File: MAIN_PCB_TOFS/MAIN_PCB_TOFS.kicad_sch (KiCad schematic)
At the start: 0 parts

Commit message: ajout de quelques éléments au pcb
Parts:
- added D4: GREEN_LED, LED_SMD:LED_0603_1608Metric, symbol Device:LED
- added D5: RED_LED, LED_SMD:LED_0603_1608Metric, symbol Device:LED
- added J1, J11, J2: Capteur Matricielle, Connector_PinHeader_2.54mm:PinHeader_1x07_P2.54mm_Vertical, symbol Connector_Generic:Conn_01x07
- added J12: SERVO m3, Connector_PinHeader_2.54mm:PinHeader_1x03_P2.54mm_Vertical, symbol Connector:Conn_01x03_Pin
- added J13: SERVO m4, Connector_PinHeader_2.54mm:PinHeader_1x03_P2.54mm_Vertical, symbol Connector:Conn_01x03_Pin
- added J3: SERVO m2, Connector_PinHeader_2.54mm:PinHeader_1x03_P2.54mm_Vertical, symbol Connector:Conn_01x03_Pin
- added J4: SERVO m1, Connector_PinHeader_2.54mm:PinHeader_1x03_P2.54mm_Vertical, symbol Connector:Conn_01x03_Pin
- added J5: COMM_inter_mcu, Connector_PinSocket_2.54mm:PinSocket_1x09_P2.54mm_Vertical, symbol Connector:Conn_01x09_Pin
- added R12, R13: 330R, Resistor_SMD:R_0603_1608Metric, symbol Device:R
- added U1: ESP32, composant_pami:esp32_wroom32, symbol ESP_32_ANGE:ESP_32_WROOM32
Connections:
- new net: D4.2 (A), R12.2
- new net: D5.2 (A), R13.2
- new net 3V3: J1.5 (Pin_5), J11.5 (Pin_5), J2.5 (Pin_5), J5.9 (Pin_9), U1.16 (3V3)
- new net 6V: J12.2 (Pin_2), J13.2 (Pin_2), J3.2 (Pin_2), J4.2 (Pin_2), J5.8 (Pin_8)
- new net CIN1: J5.6 (Pin_6), U1.10 (D32)
- new net CIN2: J5.5 (Pin_5), U1.9 (D33)
- new net D18: J12.1 (Pin_1), J3.1 (Pin_1)
- new net D19: J13.1 (Pin_1), J4.1 (Pin_1)
- new net DIN1: J5.4 (Pin_4), U1.8 (D25)
- new net DIN2: J5.3 (Pin_3), U1.7 (D26)
- new net GND: D4.1 (K), D5.1 (K), J1.7 (Pin_7), J11.7 (Pin_7), J12.3 (Pin_3), J13.3 (Pin_3), J2.7 (Pin_7), J3.3 (Pin_3), J4.3 (Pin_3), J5.7 (Pin_7), U1.17 (GND), U1.2 (GND)
- new net LED_IHM_1: R12.1, U1.6 (D27)
- new net LED_IHM_2: R13.1, U1.5 (D14)
- new net RX_ESP32: J5.2 (Pin_2), U1.21 (RX2)
- new net SCL: J1.2 (Pin_2), J11.2 (Pin_2), J2.2 (Pin_2), U1.29 (D22)
- new net SDA: J1.1 (Pin_1), J11.1 (Pin_1), J2.1 (Pin_1), U1.26 (D21)
- new net SERVO_1: U1.25 (D19)
- new net SERVO_2: U1.24 (D18)
- new net SERVO_3: U1.19 (D2)
- new net SERVO_4: U1.18 (D15)
- new net TX_ESP32: J5.1 (Pin_1), U1.22 (TX2)
- no-connect marks 0 -> 12
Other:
- note added: "Capteur TOF 1"
- note added: "Capteur TOF 2"
- note added: "Capteur TOF 3"
- note added: "Servo Moteur 1"
- note added: "Servo Moteur 2"
- note added: "Servo Moteur 3"
- note added: "Servo Moteur 4"

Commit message: début du schéma électrique
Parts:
- U1: footprint composant_pami:esp32_wroom32 -> Library:PinHeader_2x15_P2.54mm_Vertical_esp32
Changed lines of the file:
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@@
 			)
 		)
-		(property "Footprint" "composant_pami:esp32_wroom32"
+		(property "Footprint" "Library:PinHeader_2x15_P2.54mm_Vertical_esp32"
 			(at 85.09 44.45 0)
 			(effects

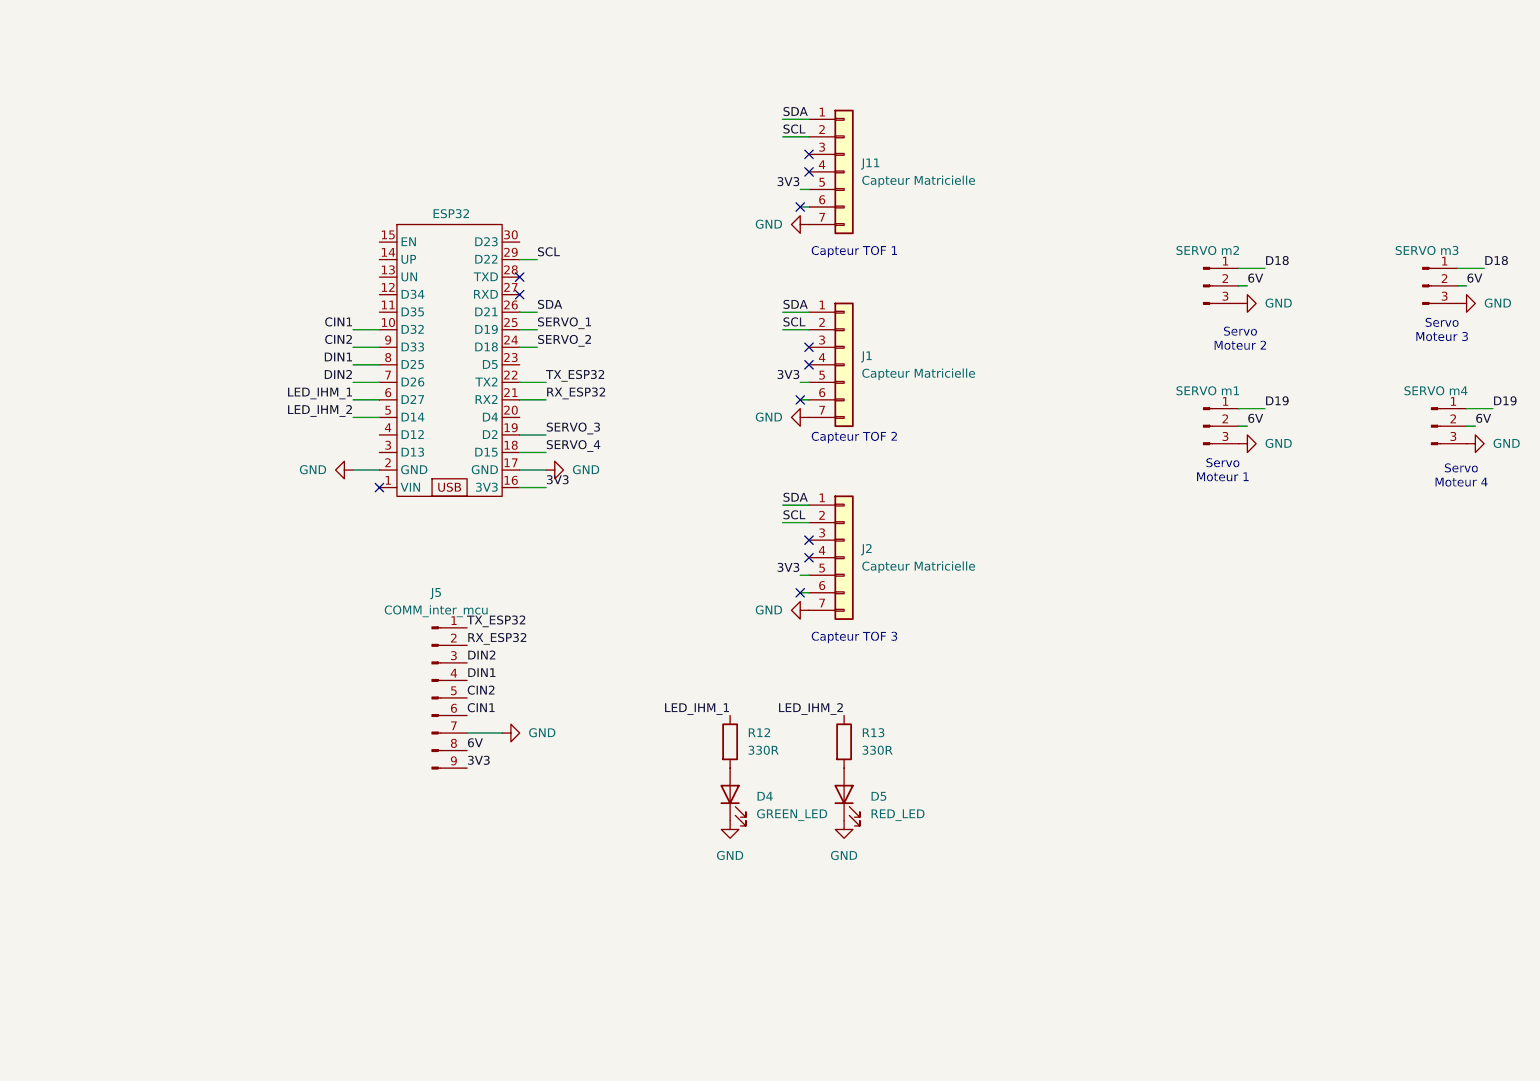
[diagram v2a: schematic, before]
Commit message: ajout des switch, des tofs et mise en place des capa de découplage sur le pcb logique
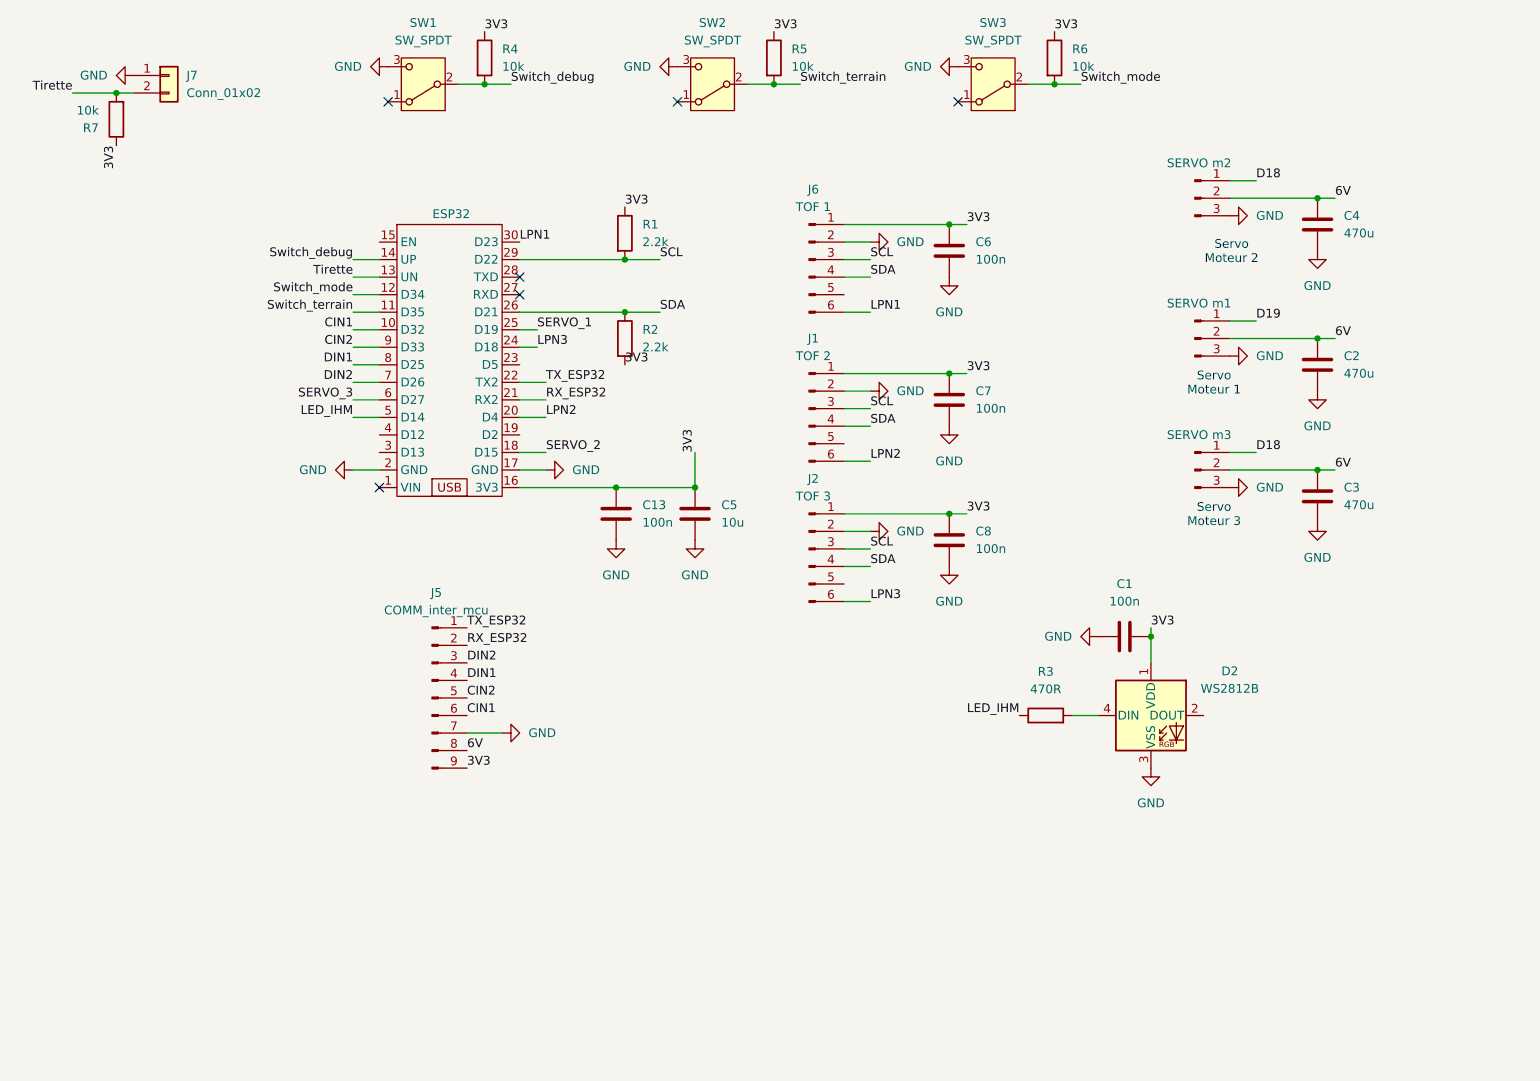
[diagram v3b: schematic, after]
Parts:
- removed D4: GREEN_LED, LED_SMD:LED_0603_1608Metric, symbol Device:LED
- removed D5: RED_LED, LED_SMD:LED_0603_1608Metric, symbol Device:LED
- removed J1, J11, J2: Capteur Matricielle, Connector_PinHeader_2.54mm:PinHeader_1x07_P2.54mm_Vertical, symbol Connector_Generic:Conn_01x07
- removed J13: SERVO m4, Connector_PinHeader_2.54mm:PinHeader_1x03_P2.54mm_Vertical, symbol Connector:Conn_01x03_Pin
- removed R12, R13: 330R, Resistor_SMD:R_0603_1608Metric, symbol Device:R
- added C1: 100n, symbol Device:C
- added C13, C6, C7, C8: 100n, Capacitor_SMD:C_0603_1608Metric, symbol Device:C
- added C2, C3, C4: 470u, symbol Device:C
- added C5: 10u, Capacitor_SMD:C_0603_1608Metric, symbol Device:C
- added D2: WS2812B, LED_SMD:LED_WS2812B_PLCC4_5.0x5.0mm_P3.2mm, symbol LED:WS2812B
- added J1: TOF 2, symbol Connector:Conn_01x06_Pin
- added J2: TOF 3, symbol Connector:Conn_01x06_Pin
- added J6: TOF 1, symbol Connector:Conn_01x06_Pin
- added J7: Conn_01x02, symbol Connector_Generic:Conn_01x02
- added R1, R2: 2.2k, symbol Device:R
- added R3: 470R, symbol Device:R
- added R4, R5, R6, R7: 10k, symbol Device:R
- added SW1, SW2, SW3: SW_SPDT, Button_Switch_SMD:SW_SPDT_PCM12, symbol Switch:SW_SPDT
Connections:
- net LED_IHM_1 is gone; now on net SERVO_3: U1.6 (D27)
- net SERVO_4 is gone; now on net SERVO_2: U1.18 (D15)
- net 3V3: now also C1.2, C13.1, C5.1, C6.1, C7.1, C8.1, D2.1 (VDD), J1.1 (Pin_1), J2.1 (Pin_1), J6.1 (Pin_1), R1.1, R2.2, R4.1, R5.1, R6.1, R7.1
- net 6V: now also C2.1, C3.1, C4.1
- net GND: now also C1.1, C13.2, C2.2, C3.2, C4.2, C5.2, C6.2, C7.2, C8.2, D2.3 (VSS), J1.2 (Pin_2), J2.2 (Pin_2), J6.2 (Pin_2), J7.1 (Pin_1), SW1.3 (C), SW2.3 (C), SW3.3 (C)
- net SCL: now also J1.3 (Pin_3), J2.3 (Pin_3), J6.3 (Pin_3), R1.2
- net SDA: now also J1.4 (Pin_4), J2.4 (Pin_4), J6.4 (Pin_4), R2.1
- net SERVO_2: no longer U1.24 (D18)
- net SERVO_3: no longer U1.19 (D2)
- net Switch_terrain: now reaches U1.11 (D35)
- net Switch_terrain: now also R5.2, SW2.2 (B)
- net Switch_mode: now reaches U1.12 (D34)
- net Switch_mode: now also R6.2, SW3.2 (B)
- net Tirette: now reaches U1.13 (UN)
- net Tirette: now also J7.2 (Pin_2), R7.2
- net Switch_debug: now reaches U1.14 (UP)
- net Switch_debug: now also R4.2, SW1.2 (B)
- net LPN2: now reaches U1.20 (D4)
- net LPN2: now also J1.6 (Pin_6)
- net LPN1: now reaches U1.30 (D23)
- net LPN1: now also J6.6 (Pin_6)
- net LED_IHM_2 renamed LED_IHM
- net LED_IHM: now also R3.1
- new net: D2.4 (DIN), R3.2
- new net LPN3: J2.6 (Pin_6), U1.24 (D18)
- no-connect marks 12 -> 6
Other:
- note removed: "Capteur TOF 1"
- note removed: "Capteur TOF 2"
- note removed: "Capteur TOF 3"
- note removed: "Servo Moteur 4"

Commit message: petites modifs kicad
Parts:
- C1: footprint (none) -> Capacitor_SMD:C_0603_1608Metric
- C2, C3, C4: value 470u -> 100u; footprint (none) -> Capacitor_SMD:CP_Elec_6.3x5.8
- J1, J2, J6: footprint (none) -> Connector_PinHeader_2.54mm:PinHeader_1x06_P2.54mm_Vertical
- J7: footprint (none) -> Connector_PinHeader_2.54mm:PinHeader_1x02_P2.54mm_Vertical
- R1, R2, R3, R4, R5, R6, R7: footprint (none) -> Resistor_SMD:R_0603_1608Metric
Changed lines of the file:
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@@
 			)
 		)
-		(property "Footprint" ""
+		(property "Footprint" "Resistor_SMD:R_0603_1608Metric"
 			(at 38.608 44.45 90)
 			(effects
@@
 			)
 		)
-		(property "Footprint" ""
+		(property "Footprint" "Connector_PinHeader_2.54mm:PinHeader_1x02_P2.54mm_Vertical"
 			(at 44.45 38.1 0)
 			(effects
@@
 			)
 		)
-		(property "Footprint" ""
+		(property "Footprint" "Connector_PinHeader_2.54mm:PinHeader_1x06_P2.54mm_Vertical"
 			(at 137.16 106.68 0)
 			(effects
@@
 			)
 		)
-		(property "Footprint" ""
+		(property "Footprint" "Resistor_SMD:R_0603_1608Metric"
 			(at 170.942 35.56 90)
 			(effects
@@
 			)
 		)
-		(property "Footprint" ""
+		(property "Footprint" "Capacitor_SMD:C_0603_1608Metric"
 			(at 186.69 118.4148 0)
 			(effects
@@
 			)
 		)
-		(property "Value" "470u"
+		(property "Value" "100u"
 			(at 214.63 81.2799 0)
 			(effects
@@
 			)
 		)
-		(property "Footprint" ""
+		(property "Footprint" "Capacitor_SMD:CP_Elec_6.3x5.8"
 			(at 211.7852 83.82 0)
 			(effects
@@
 			)
 		)
-		(property "Footprint" ""
+		(property "Footprint" "Connector_PinHeader_2.54mm:PinHeader_1x06_P2.54mm_Vertical"
 			(at 137.16 86.36 0)
 			(effects
@@
 			)
 		)
-		(property "Value" "470u"
+		(property "Value" "100u"
 			(at 214.63 60.9599 0)
 			(effects
@@
 			)
 		)
-		(property "Footprint" ""
+		(property "Footprint" "Capacitor_SMD:CP_Elec_6.3x5.8"
 			(at 211.7852 63.5 0)
 			(effects
@@
 			)
 		)
-		(property "Value" "470u"
+		(property "Value" "100u"
 			(at 214.63 100.3299 0)
 			(effects
@@
 			)
 		)
-		(property "Footprint" ""
+		(property "Footprint" "Capacitor_SMD:CP_Elec_6.3x5.8"
 			(at 211.7852 102.87 0)
 			(effects
@@
 			)
 		)
-		(property "Footprint" ""
+		(property "Footprint" "Connector_PinHeader_2.54mm:PinHeader_1x06_P2.54mm_Vertical"
 			(at 137.16 64.77 0)
 			(effects
@@
 			)
 		)
-		(property "Footprint" ""
+		(property "Footprint" "Resistor_SMD:R_0603_1608Metric"
 			(at 108.712 60.96 90)
 			(effects
@@
 			)
 		)
-		(property "Footprint" ""
+		(property "Footprint" "Resistor_SMD:R_0603_1608Metric"
 			(at 88.392 35.56 90)
 			(effects
@@
 			)
 		)
-		(property "Footprint" ""
+		(property "Footprint" "Resistor_SMD:R_0603_1608Metric"
 			(at 130.302 35.56 90)
 			(effects
@@
 			)
 		)
-		(property "Footprint" ""
+		(property "Footprint" "Resistor_SMD:R_0603_1608Metric"
 			(at 171.45 132.588 90)
 			(effects
@@
 			)
 		)
-		(property "Footprint" ""
+		(property "Footprint" "Resistor_SMD:R_0603_1608Metric"
 			(at 108.712 76.2 90)
 			(effects

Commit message: organisation du pcb IHM pour préparer le routage
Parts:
- added H1, H2, H3, H4: MountingHole_Pad, MountingHole:MountingHole_3.2mm_M3_Pad_Via, symbol Mechanical:MountingHole_Pad
- SW1: value SW_SPDT -> DEBUG
- SW2: value SW_SPDT -> TERRAIN
- SW3: value SW_SPDT -> MODE
- U1: footprint Library:PinHeader_2x15_P2.54mm_Vertical_esp32 -> Library:DIP-30_W25.4mm_LongPads_esp32
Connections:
- net D19 is gone; now on net SERVO_1: J4.1 (Pin_1)
- net GND: now also H1.1, H2.1, H3.1, H4.1
- net LPN1: now also U1.20 (D4); no longer U1.30 (D23)
- net LPN2: now also U1.30 (D23); no longer U1.20 (D4)
- net SERVO_2: now also J3.1 (Pin_1)
- net SERVO_3: now also J12.1 (Pin_1)
- removed net D18: J12.1 (Pin_1), J3.1 (Pin_1)

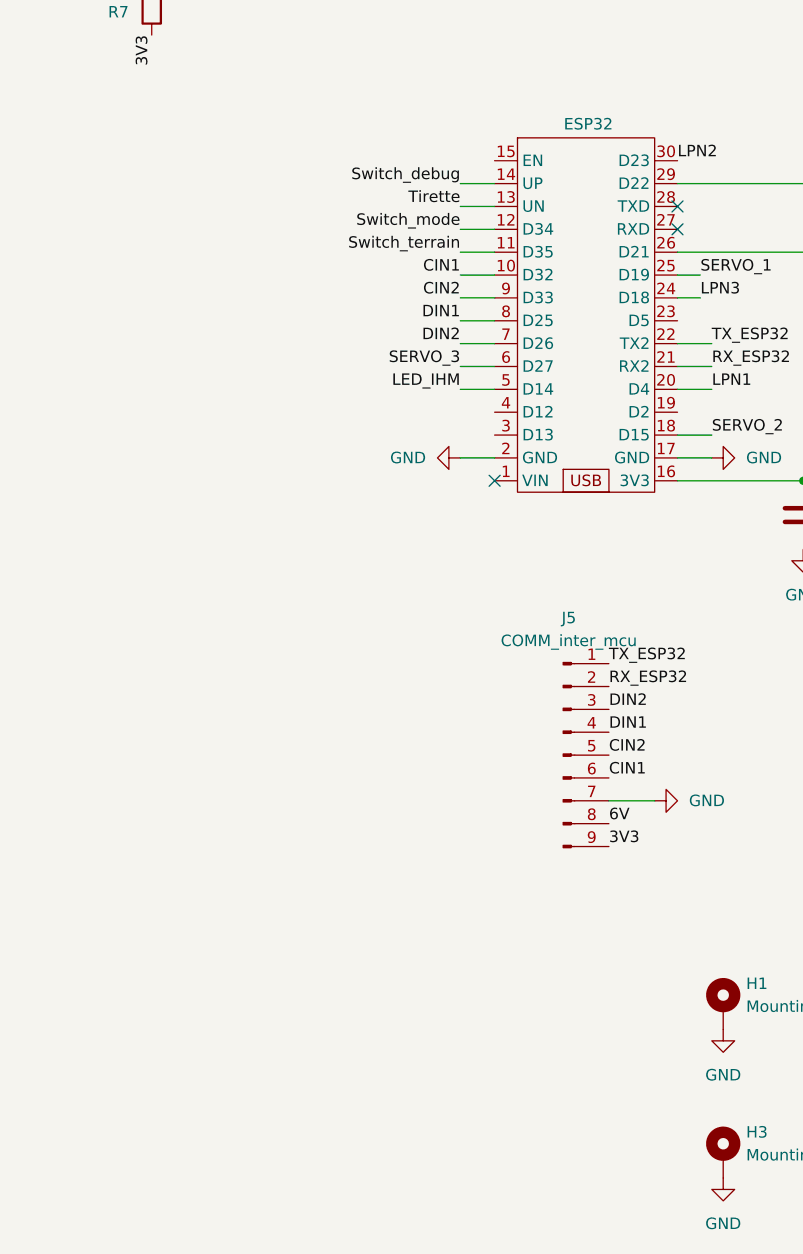
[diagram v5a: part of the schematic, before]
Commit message: modifications finales du pcb, problème sens capteurs tofs à régler
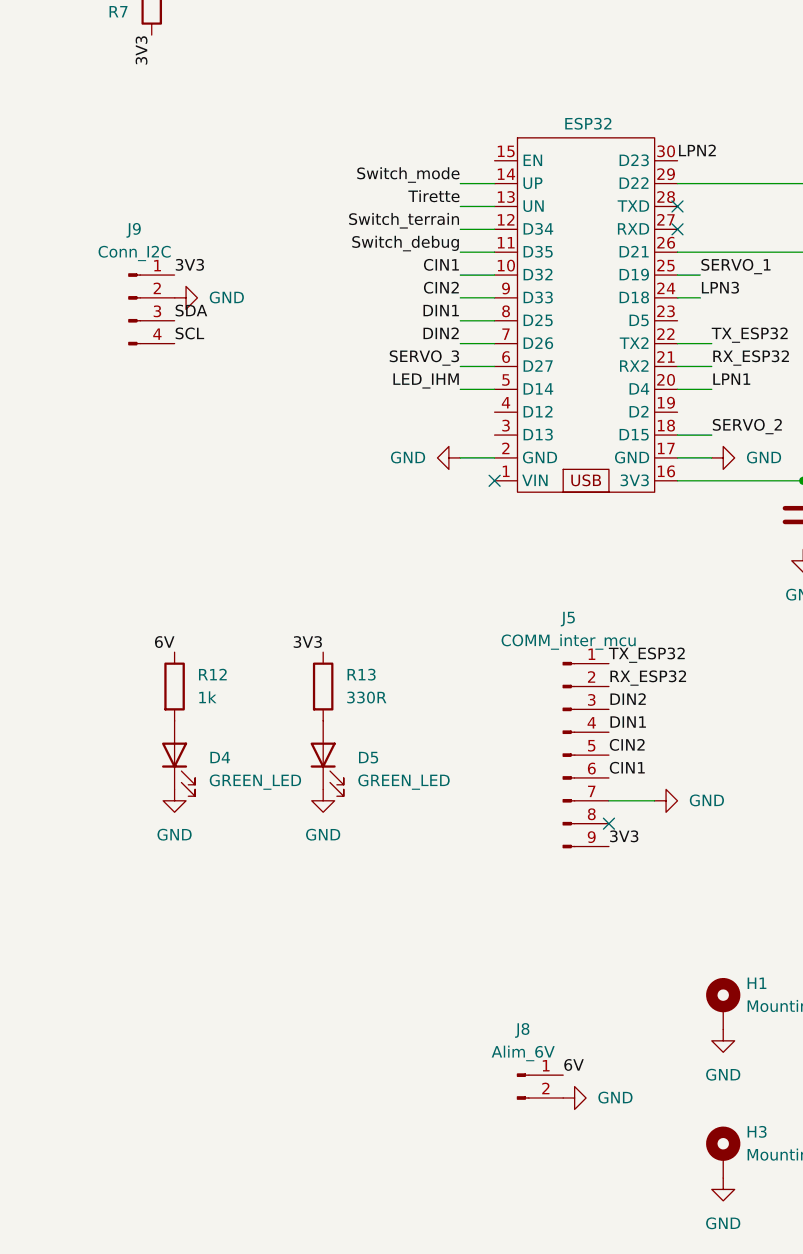
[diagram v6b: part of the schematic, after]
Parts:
- added D4, D5: GREEN_LED, LED_SMD:LED_0603_1608Metric, symbol Device:LED
- added J8: Alim_6V, Connector_JST:JST_VH_B2P-VH_1x02_P3.96mm_Vertical, symbol Connector:Conn_01x02_Pin
- added J9: Conn_I2C, Connector_PinHeader_2.54mm:PinHeader_1x04_P2.54mm_Vertical, symbol Connector:Conn_01x04_Pin
- added R12: 1k, Resistor_SMD:R_0603_1608Metric, symbol Device:R
- added R13: 330R, Resistor_SMD:R_0603_1608Metric, symbol Device:R
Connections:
- net 3V3: now also J9.1 (Pin_1), R13.1
- net 6V: now also J8.1 (Pin_1), R12.1; no longer J5.8 (Pin_8)
- net GND: now also D4.1 (K), D5.1 (K), J8.2 (Pin_2), J9.2 (Pin_2)
- net SCL: now also J9.4 (Pin_4)
- net SDA: now also J9.3 (Pin_3)
- net Switch_debug: now also U1.11 (D35); no longer U1.14 (UP)
- net Switch_mode: now also U1.14 (UP); no longer U1.12 (D34)
- net Switch_terrain: now also U1.12 (D34); no longer U1.11 (D35)
- new net: D4.2 (A), R12.2
- new net: D5.2 (A), R13.2
- no-connect marks 6 -> 7
